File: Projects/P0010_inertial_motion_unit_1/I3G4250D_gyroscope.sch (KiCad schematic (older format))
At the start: 19 parts, among them J1 modular8_rev3_comms_in, J2 modular8_rev3_comms_out, U1 I3G4250DTR, U2 ADXL343

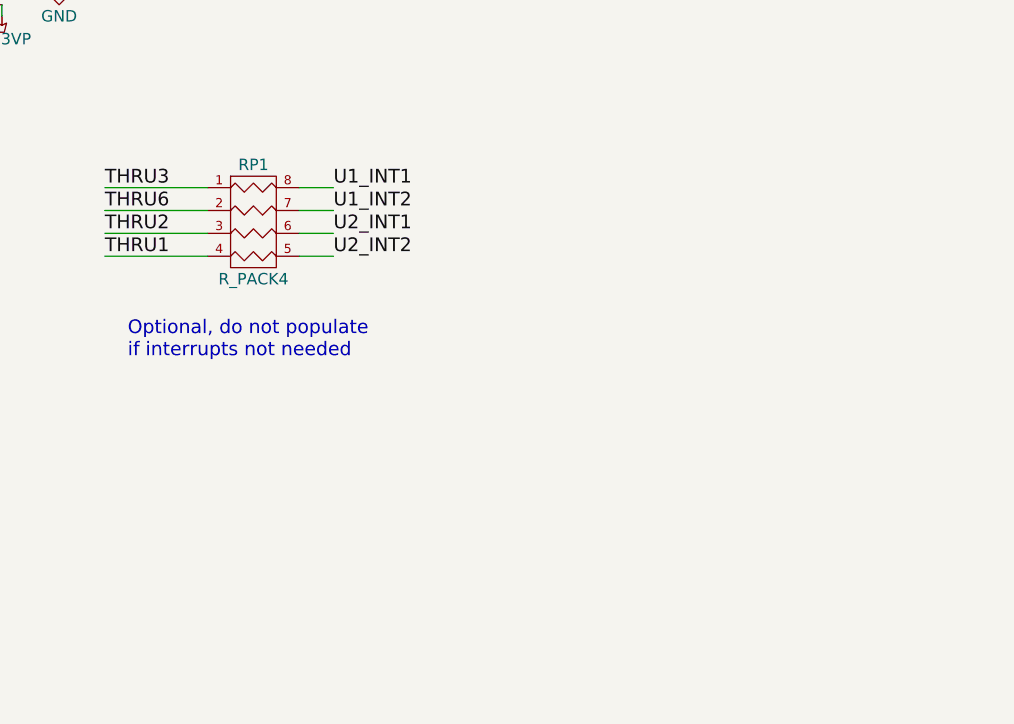
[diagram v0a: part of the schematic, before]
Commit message: moved gyro/accel to Projects
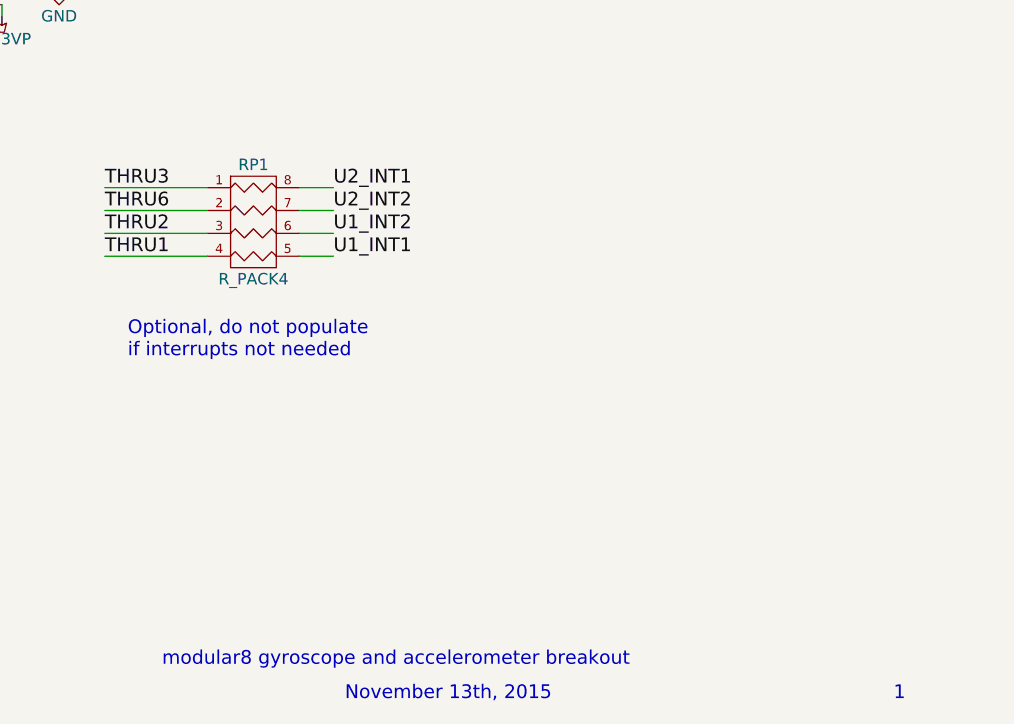
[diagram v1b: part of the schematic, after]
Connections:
- net U1_INT1: now also RP1.5 (R4); no longer RP1.8 (R1)
- net U1_INT2: now also RP1.6 (R3); no longer RP1.7 (R2)
- net U2_INT1: now also RP1.8 (R1); no longer RP1.6 (R3)
- net U2_INT2: now also RP1.7 (R2); no longer RP1.5 (R4)
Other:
- note added: "1"
- note added: "November 13th, 2015"
- note added: "modular8 gyroscope and accelerometer breakout"
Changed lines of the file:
@@
 LIBS:contrib
 LIBS:valves
-LIBS:open_robotics
 LIBS:I3G4250D_gyroscope-cache
 EELAYER 25 0
@@
 	1    0    0    -1
 $EndComp
+Text Label 8100 5700 0    60   ~ 0
+U1_INT1
+Text Label 8100 5600 0    60   ~ 0
+U1_INT2
 Text Label 8100 5400 0    60   ~ 0
-U1_INT1
+U2_INT1
 Text Label 8100 5500 0    60   ~ 0
-U1_INT2
-Text Label 8100 5600 0    60   ~ 0
-U2_INT1
-Text Label 8100 5700 0    60   ~ 0
 U2_INT2
 Wire Wire Line
@@
 	1650 3000 1650 3500
 Connection ~ 1650 3250
+Text Notes 7350 7500 0    60   ~ 0
+modular8 gyroscope and accelerometer breakout
+Text Notes 8150 7650 0    60   ~ 0
+November 13th, 2015
+Text Notes 10550 7650 0    60   ~ 0
+1
 $EndSCHEMATC

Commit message: generated gerbers, ordered P0010
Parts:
- C1, C2, C3, C4, C5, C6, C7, C8, C9: footprint Capacitors_SMD:C_0805 -> Capacitors_SMD:C_0603
- J1: footprint Libraries - KiCAD:modular8_rev3_edge -> open_robotics:modular8_rev3_edge
- J2: footprint Libraries - KiCAD:modular8_rev3_edge -> open_robotics:modular8_rev3_edge; symbol modular8_rev3_comms_out -> modular8_rev3_comms_out-RESCUE-I3G4250D_gyroscope
- LDO1, LDO2: symbol AP7313-33SAG-7 -> AP7313-33SAG-7-RESCUE-I3G4250D_gyroscope
- R1, R2: footprint Resistors_SMD:R_0805 -> Resistors_SMD:R_0603
- U1: footprint Libraries - KiCAD:LGA-16 -> open_robotics:LGA-16
- U2: footprint Libraries - KiCAD:LGACC-14-1 -> open_robotics:LGACC-14-1
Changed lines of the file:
@@
 EESchema Schematic File Version 2
+LIBS:I3G4250D_gyroscope-rescue
 LIBS:power
 LIBS:device
@@
 LIBS:contrib
 LIBS:valves
+LIBS:open_robotics
 LIBS:I3G4250D_gyroscope-cache
 EELAYER 25 0
@@
 F 0 "U1" H 1750 5100 60  0000 C CNN
 F 1 "I3G4250DTR" H 3250 5050 60  0000 C CNN
-F 2 "Libraries - KiCAD:LGA-16" H 2300 4450 60  0001 C CNN
+F 2 "open_robotics:LGA-16" H 2300 4450 60  0001 C CNN
 F 3 "" H 2300 4450 60  0000 C CNN
 	1    2300 4450
@@
 F 0 "C1" V 1800 2850 50  0000 L CNN
 F 1 "10nF" V 1800 3000 50  0000 L CNN
-F 2 "Capacitors_SMD:C_0805" H 1988 2850 30  0001 C CNN
+F 2 "Capacitors_SMD:C_0603" H 1988 2850 30  0001 C CNN
 F 3 "" H 1950 3000 60  0000 C CNN
 	1    1950 3000
@@
 F 0 "C2" V 2050 3450 50  0000 L CNN
 F 1 "0.47uF" V 2150 3450 50  0000 L CNN
-F 2 "Capacitors_SMD:C_0805" H 2138 3100 30  0001 C CNN
+F 2 "Capacitors_SMD:C_0603" H 2138 3100 30  0001 C CNN
 F 3 "" H 2100 3250 60  0000 C CNN
 	1    2100 3250
@@
 F 0 "U2" H 5100 4750 60  0000 C CNN
 F 1 "ADXL343" H 6250 4750 60  0000 C CNN
-F 2 "Libraries - KiCAD:LGACC-14-1" H 5400 4900 60  0001 C CNN
+F 2 "open_robotics:LGACC-14-1" H 5400 4900 60  0001 C CNN
 F 3 "" H 5400 4900 60  0000 C CNN
 	1    5750 4350
@@
 F 0 "C8" H 9575 3300 50  0000 L CNN
 F 1 "0.1uF" H 9575 3100 50  0000 L CNN
-F 2 "Capacitors_SMD:C_0805" H 9588 3050 30  0001 C CNN
+F 2 "Capacitors_SMD:C_0603" H 9588 3050 30  0001 C CNN
 F 3 "" H 9550 3200 60  0000 C CNN
 	1    9550 3200
@@
 F 0 "R1" V 1880 3250 50  0000 C CNN
 F 1 "10k" V 1800 3250 50  0000 C CNN
-F 2 "Resistors_SMD:R_0805" V 1730 3250 30  0001 C CNN
+F 2 "Resistors_SMD:R_0603" V 1730 3250 30  0001 C CNN
 F 3 "" H 1800 3250 30  0000 C CNN
 	1    1800 3250
@@
 F 0 "J1" H 4300 2400 60  0000 C CNN
 F 1 "modular8_rev3_comms_in" H 4000 2300 60  0000 C CNN
-F 2 "Libraries - KiCAD:modular8_rev3_edge" H 3950 1900 60  0001 C CNN
+F 2 "open_robotics:modular8_rev3_edge" H 3950 1900 60  0001 C CNN
 F 3 "" H 3950 1900 60  0000 C CNN
 	1    3950 1900
@@
 $EndComp
 $Comp
-L modular8_rev3_comms_out J2
+L modular8_rev3_comms_out-RESCUE-I3G4250D_gyroscope J2
 U 1 1 560B5AFA
 P 3950 6200
 F 0 "J2" H 4300 6700 60  0000 C CNN
 F 1 "modular8_rev3_comms_out" H 3950 6600 60  0000 C CNN
-F 2 "Libraries - KiCAD:modular8_rev3_edge" H 3950 6200 60  0001 C CNN
+F 2 "open_robotics:modular8_rev3_edge" H 3950 6200 60  0001 C CNN
 F 3 "" H 3950 6200 60  0000 C CNN
 	1    3950 6200
@@
 I2C 1010011
 $Comp
-L AP7313-33SAG-7 LDO2
+L AP7313-33SAG-7-RESCUE-I3G4250D_gyroscope LDO2
 U 1 1 560BA757
 P 8600 2950
@@
 $EndComp
 $Comp
-L AP7313-33SAG-7 LDO1
+L AP7313-33SAG-7-RESCUE-I3G4250D_gyroscope LDO1
 U 1 1 560BA8F2
 P 8600 2050
@@
 F 0 "C4" H 7975 2400 50  0000 L CNN
 F 1 "1uF" H 7975 2200 50  0000 L CNN
-F 2 "Capacitors_SMD:C_0805" H 7988 2150 30  0001 C CNN
+F 2 "Capacitors_SMD:C_0603" H 7988 2150 30  0001 C CNN
 F 3 "" H 7950 2300 60  0000 C CNN
 	1    7950 2300
@@
 F 0 "C3" H 7675 3300 50  0000 L CNN
 F 1 "1uF" H 7675 3100 50  0000 L CNN
-F 2 "Capacitors_SMD:C_0805" H 7688 3050 30  0001 C CNN
+F 2 "Capacitors_SMD:C_0603" H 7688 3050 30  0001 C CNN
 F 3 "" H 7650 3200 60  0000 C CNN
 	1    7650 3200
@@
 F 0 "C5" H 9225 2400 50  0000 L CNN
 F 1 "1uF" H 9225 2200 50  0000 L CNN
-F 2 "Capacitors_SMD:C_0805" H 9238 2150 30  0001 C CNN
+F 2 "Capacitors_SMD:C_0603" H 9238 2150 30  0001 C CNN
 F 3 "" H 9200 2300 60  0000 C CNN
 	1    9200 2300
@@
 F 0 "C6" H 9225 3300 50  0000 L CNN
 F 1 "1uF" H 9225 3100 50  0000 L CNN
-F 2 "Capacitors_SMD:C_0805" H 9238 3050 30  0001 C CNN
+F 2 "Capacitors_SMD:C_0603" H 9238 3050 30  0001 C CNN
 F 3 "" H 9200 3200 60  0000 C CNN
 	1    9200 3200
@@
 F 0 "C7" H 9575 2400 50  0000 L CNN
 F 1 "10uF tantalum" H 9575 2200 50  0000 L CNN
-F 2 "Capacitors_SMD:C_0805" H 9588 2150 30  0001 C CNN
+F 2 "Capacitors_SMD:C_0603" H 9588 2150 30  0001 C CNN
 F 3 "" H 9550 2300 60  0000 C CNN
 	1    9550 2300
@@
 F 0 "C9" H 9925 3300 50  0000 L CNN
 F 1 "0.1uF" H 9925 3100 50  0000 L CNN
-F 2 "Capacitors_SMD:C_0805" H 9938 3050 30  0001 C CNN
+F 2 "Capacitors_SMD:C_0603" H 9938 3050 30  0001 C CNN
 F 3 "" H 9900 3200 60  0000 C CNN
 	1    9900 3200
@@
 F 0 "R2" V 7430 2850 50  0000 C CNN
 F 1 "680" V 7350 2850 50  0000 C CNN
-F 2 "Resistors_SMD:R_0805" V 7280 2850 30  0001 C CNN
+F 2 "Resistors_SMD:R_0603" V 7280 2850 30  0001 C CNN
 F 3 "" H 7350 2850 30  0000 C CNN
 	1    7350 2850
